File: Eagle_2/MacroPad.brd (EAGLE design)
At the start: 76.2 x 76.2 mm, 42 parts, among them SW00 SWITCH-SMD-EVQP-P2602W, SW01 KEYSWITCH-PLAIN-MX-1U, SW02 KEYSWITCH-PLAIN-MX-1U, SW03 KEYSWITCH-PLAIN-MX-1U, SW04 KEYSWITCH-PLAIN-MX-1U, SW05 KEYSWITCH-PLAIN-MX-1U, SW06 KEYSWITCH-PLAIN-MX-1U, SW07 KEYSWITCH-PLAIN-MX-1U, SW08 KEYSWITCH-PLAIN-MX-1U, SW09 KEYSWITCH-PLAIN-MX-1U, SW10 KEYSWITCH-PLAIN-MX-1U, SW11 KEYSWITCH-PLAIN-MX-1U, SW12 KEYSWITCH-PLAIN-MX-1U

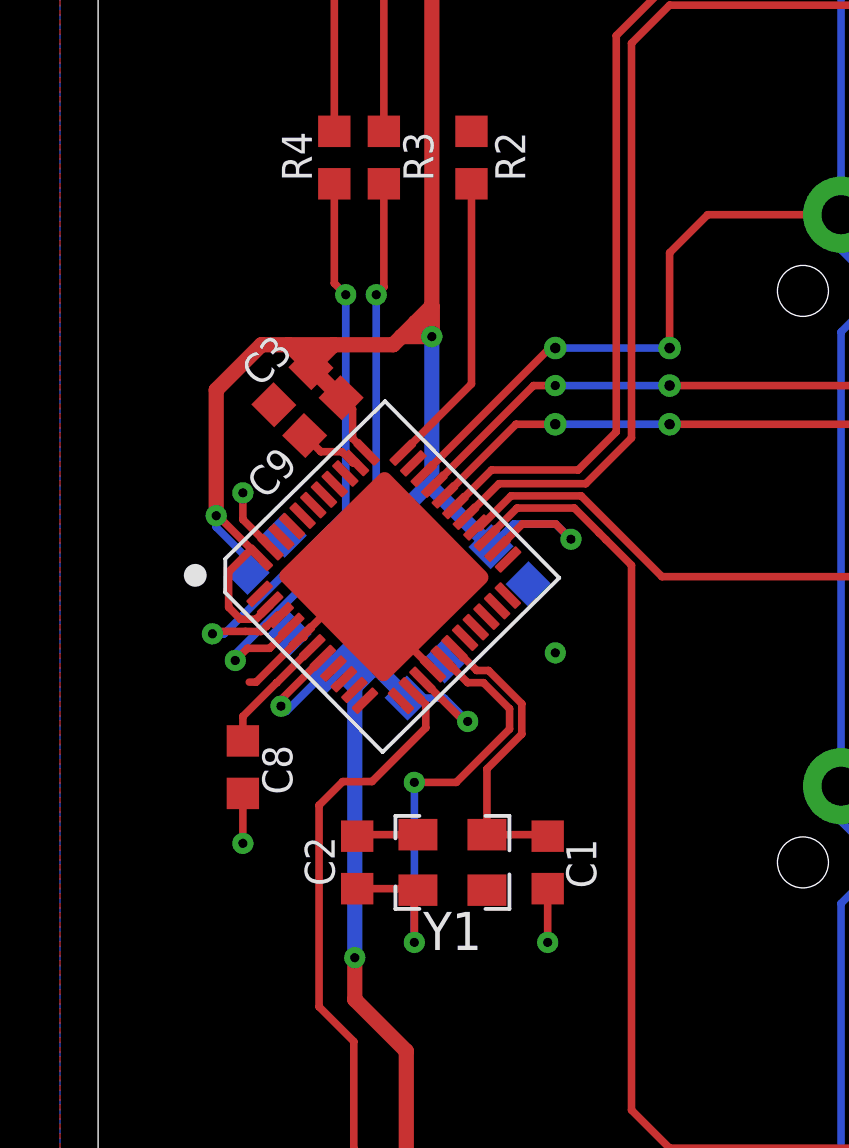
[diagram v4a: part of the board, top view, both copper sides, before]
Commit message: Adjust vias position based on JLCPCB rendering
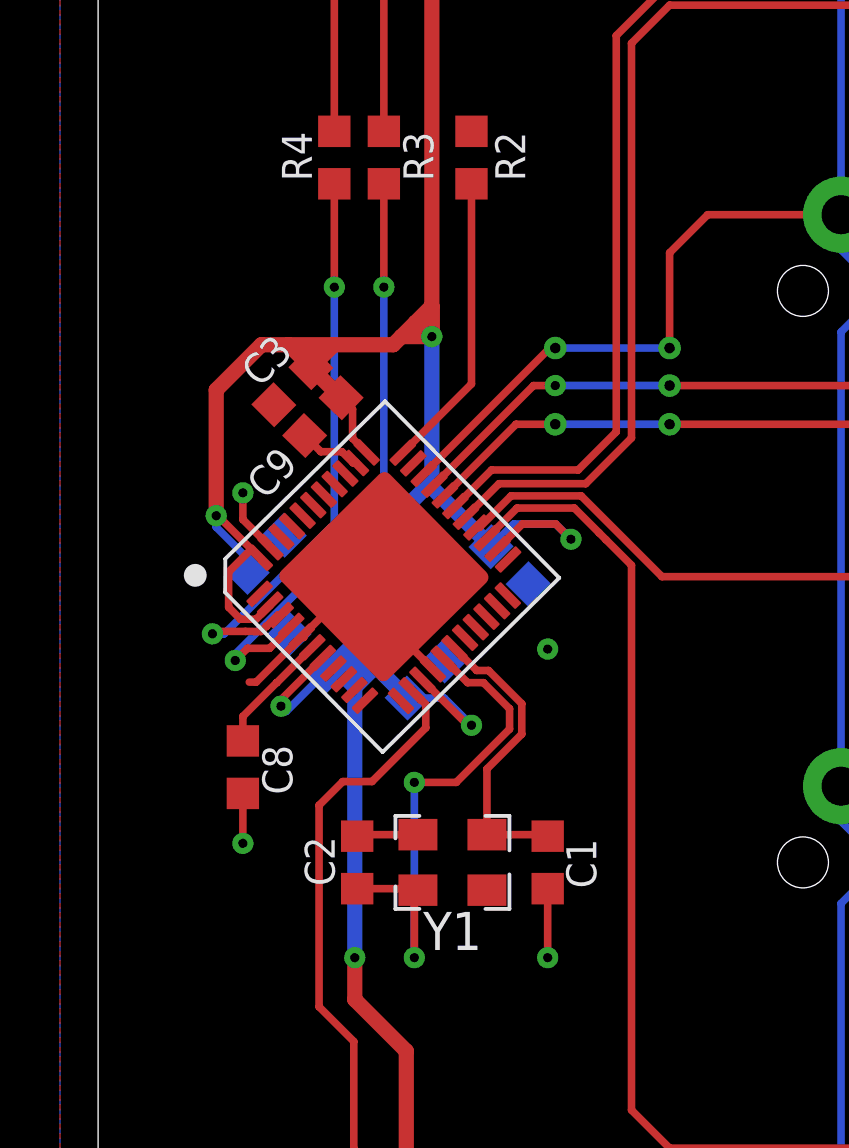
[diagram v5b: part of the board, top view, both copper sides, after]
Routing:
- net N$1: track 16.6 -> 17.7 mm
- net GND: track 23.5 -> 24.0 mm
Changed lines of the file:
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@@
 <wire x1="11.938" y1="31.242" x2="10.541" y2="31.242" width="0.254" layer="1"/>
 <via x="10.541" y="31.242" extent="1-16" drill="0.3048"/>
-<wire x1="10.541" y1="31.242" x2="10.541" y2="25.908" width="0.254" layer="16"/>
-<via x="10.541" y="25.908" extent="1-16" drill="0.3048"/>
+<wire x1="10.541" y1="31.242" x2="10.541" y2="25.4" width="0.254" layer="16"/>
+<via x="10.541" y="25.4" extent="1-16" drill="0.3048"/>
 <wire x1="10.661" y1="27.65" x2="10.541" y2="27.53" width="0.254" layer="1"/>
-<wire x1="10.541" y1="27.53" x2="10.541" y2="25.908" width="0.254" layer="1"/>
+<wire x1="10.541" y1="27.53" x2="10.541" y2="25.4" width="0.254" layer="1"/>
 <wire x1="8.636" y1="27.7" x2="10.611" y2="27.7" width="0.254" layer="1"/>
 <wire x1="10.611" y1="27.7" x2="10.661" y2="27.65" width="0.254" layer="1"/>
@@
 <wire x1="15.253734375" y1="39.855403125" x2="13.852971875" y2="39.855403125" width="0.254" layer="16"/>
 <wire x1="13.852971875" y1="39.855403125" x2="13.097284375" y2="39.099715625" width="0.254" layer="16"/>
-<wire x1="10.809171875" y1="34.66148125" x2="12.196653125" y2="33.274" width="0.254" layer="1"/>
-<wire x1="12.196653125" y1="33.274" x2="12.319" y2="33.274" width="0.254" layer="1"/>
-<via x="12.319" y="33.274" extent="1-16" drill="0.3048"/>
+<wire x1="10.809171875" y1="34.66148125" x2="12.323653125" y2="33.147" width="0.254" layer="1"/>
+<wire x1="12.323653125" y1="33.147" x2="12.446" y2="33.147" width="0.254" layer="1"/>
+<via x="12.446" y="33.147" extent="1-16" drill="0.3048"/>
 <wire x1="7.4907875" y1="35.391771875" x2="6.096" y2="33.996984375" width="0.254" layer="1"/>
 <wire x1="6.096" y1="33.996984375" x2="6.096" y2="33.782" width="0.254" layer="1"/>
@@
 <wire x1="11.125" y1="41.072" x2="11.125" y2="41.275" width="0.508" layer="16"/>
 <wire x1="10.303284375" y1="34.05228125" x2="11.54071875" y2="34.05228125" width="0.254" layer="16"/>
-<wire x1="11.54071875" y1="34.05228125" x2="12.319" y2="33.274" width="0.254" layer="16"/>
+<wire x1="11.54071875" y1="34.05228125" x2="12.446" y2="33.147" width="0.254" layer="16"/>
 <wire x1="11.125" y1="46.101" x2="10.109" y2="46.101" width="0.508" layer="1"/>
 <wire x1="10.109" y1="46.101" x2="9.838715625" y2="45.830715625" width="0.508" layer="1"/>
@@
 <contactref element="U$1" pad="3"/>
 <contactref element="R4" pad="2"/>
-<wire x1="7.874" y1="51.195" x2="7.874" y2="47.879" width="0.254" layer="1"/>
-<wire x1="7.874" y1="47.879" x2="8.255" y2="47.498" width="0.254" layer="1"/>
-<via x="8.255" y="47.498" extent="1-16" drill="0.3048"/>
+<wire x1="7.874" y1="51.195" x2="7.874" y2="47.752" width="0.254" layer="1"/>
+<via x="7.874" y="47.752" extent="1-16" drill="0.3048"/>
 <via x="3.81" y="36.195" extent="1-16" drill="0.3048"/>
-<wire x1="8.255" y1="47.498" x2="8.255" y2="40.243196875" width="0.254" layer="16"/>
-<wire x1="4.833896875" y1="36.82209375" x2="8.255" y2="40.243196875" width="0.254" layer="16"/>
+<wire x1="7.874" y1="47.752" x2="7.874" y2="39.862196875" width="0.254" layer="16"/>
+<wire x1="4.833896875" y1="36.82209375" x2="7.874" y2="39.862196875" width="0.254" layer="16"/>
 <wire x1="6.08648125" y1="36.815825" x2="5.985934375" y2="36.815825" width="0.254" layer="1"/>
 <wire x1="5.985934375" y1="36.815825" x2="5.6141375" y2="36.44918125" width="0.254" layer="1"/>
@@
 <contactref element="U$1" pad="4"/>
 <contactref element="R3" pad="2"/>
-<wire x1="9.271" y1="47.498" x2="9.525" y2="47.752" width="0.254" layer="1"/>
 <wire x1="9.525" y1="51.195" x2="9.525" y2="47.752" width="0.254" layer="1"/>
-<via x="9.271" y="47.498" extent="1-16" drill="0.3048"/>
-<wire x1="9.271" y1="47.498" x2="9.271" y2="40.221021875" width="0.254" layer="16"/>
+<via x="9.525" y="47.752" extent="1-16" drill="0.3048"/>
+<wire x1="9.525" y1="47.752" x2="9.525" y2="40.475021875" width="0.254" layer="16"/>
 <via x="4.572" y="35.306" extent="1-16" drill="0.3048"/>
 <wire x1="4.97816875" y1="35.71216875" x2="4.572" y2="35.306" width="0.254" layer="1"/>
@@
 <wire x1="4.97816875" y1="35.71216875" x2="5.716365625" y2="35.71216875" width="0.254" layer="1"/>
 <wire x1="4.572" y1="35.306" x2="4.57198125" y2="35.522003125" width="0.254" layer="16"/>
-<wire x1="9.271" y1="40.221021875" x2="4.57198125" y2="35.522003125" width="0.254" layer="16"/>
+<wire x1="9.525" y1="40.475021875" x2="4.57198125" y2="35.522003125" width="0.254" layer="16"/>
 </signal>
 <signal name="N$9">
@@
 <wire x1="13.335" y1="63.008" x2="13.335" y2="61.341" width="0.254" layer="1"/>
 <via x="13.335" y="61.341" extent="1-16" drill="0.3048"/>
-<wire x1="14.986" y1="27.7" x2="14.986" y2="25.908" width="0.254" layer="1"/>
-<via x="14.986" y="25.908" extent="1-16" drill="0.3048"/>
+<wire x1="14.986" y1="27.7" x2="14.986" y2="25.4" width="0.254" layer="1"/>
+<via x="14.986" y="25.4" extent="1-16" drill="0.3048"/>
 <wire x1="4.826" y1="30.875" x2="4.826" y2="29.21" width="0.254" layer="1"/>
 <via x="4.826" y="29.21" extent="1-16" drill="0.3048"/>
@@
 <vertex x="-1.27" y="-1.27"/>
 </polygon>
-<via x="15.24" y="35.56" extent="1-16" drill="0.3048"/>
+<via x="14.986" y="35.687" extent="1-16" drill="0.3048"/>
 <wire x1="8.784834375" y1="38.1" x2="8.636" y2="38.1" width="0" layer="19" extent="1-1"/>
 <wire x1="11.165184375" y1="35.012559375" x2="11.54071875" y2="34.94128125" width="0" layer="19" extent="1-16"/>
